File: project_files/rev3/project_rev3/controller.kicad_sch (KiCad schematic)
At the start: 26 parts, among them J8 USB_C_Receptacle_USB2.0_16P, SW1 JS102011SAQN, SW2 PTS810 SJM 250 SMTR LFS, SW3 PTS810 SJM 250 SMTR LFS, U5 ESP32-S3-WROOM-1-N16R8, U6 AZ1117CH-3.3

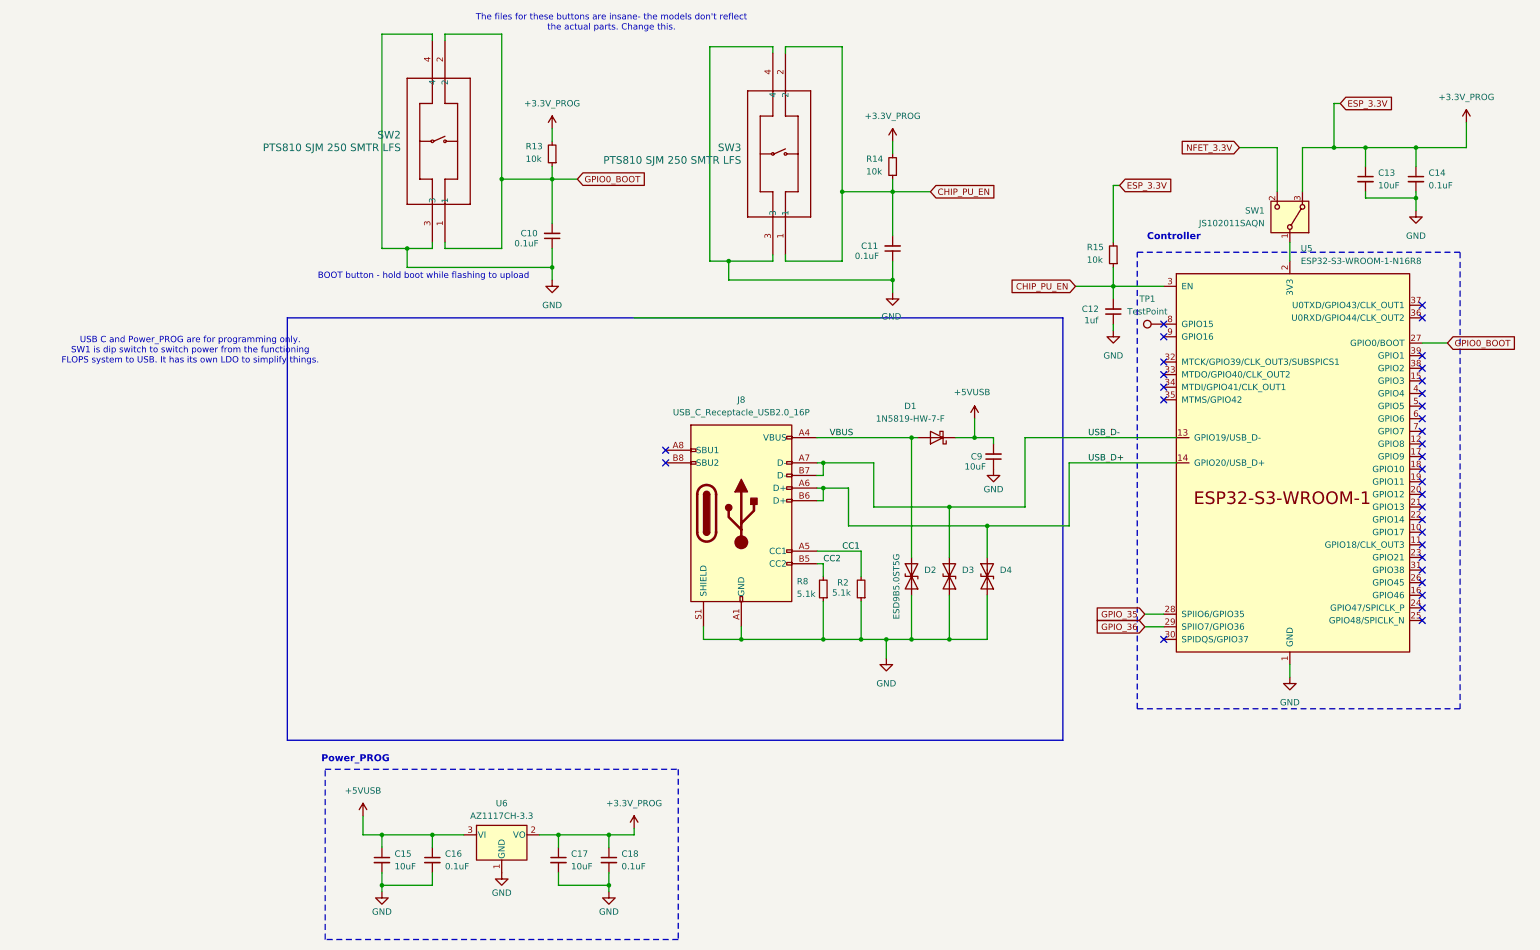
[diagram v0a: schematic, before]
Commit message: added new project for rev4 and reverted changes for rev3
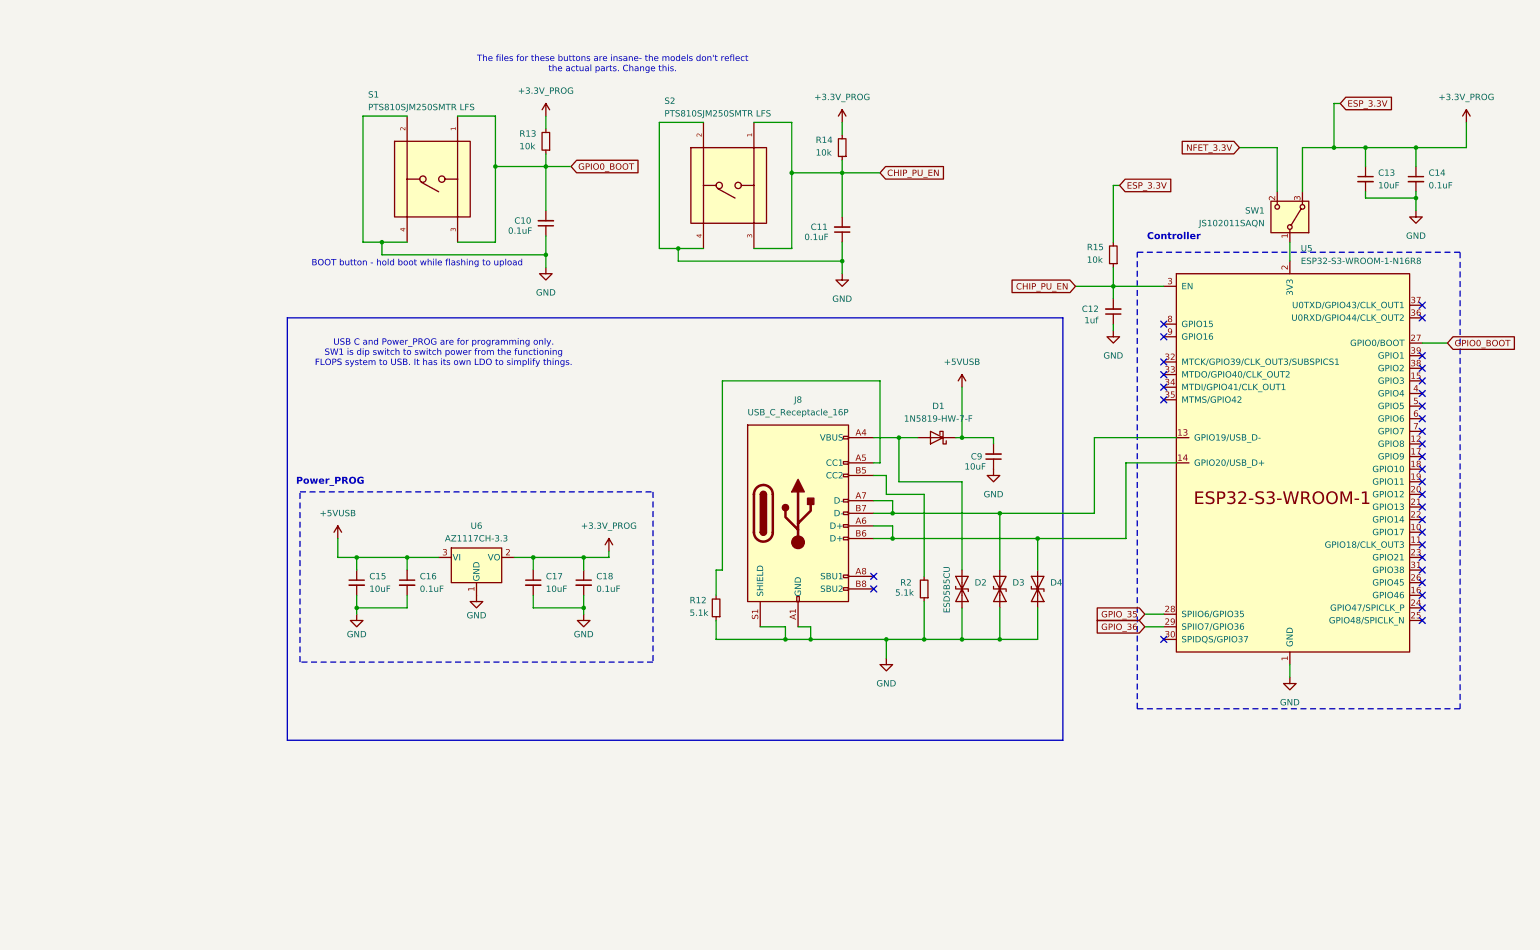
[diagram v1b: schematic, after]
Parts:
- removed R8: 5.1k, Resistor_SMD:R_0603_1608Metric_Pad0.98x0.95mm_HandSolder, symbol Device:R_Small
- removed SW2, SW3: PTS810 SJM 250 SMTR LFS, PTS810SJM250SMTR LFS:PTS810_CNK, symbol PTS810SJM250SMTR LFS:PTS810_SJM_250_SMTR_LFS
- removed TP1: TestPoint, symbol Connector:TestPoint
- added R12: 5.1k, Resistor_SMD:R_0603_1608Metric_Pad0.98x0.95mm_HandSolder, symbol Device:R_Small
- added S1, S2: PTS810SJM250SMTR LFS, TS04-66-95-BK-100-SMT:SW_TS04-66-95-BK-100-SMT, symbol TS04-66-95-BK-100-SMT:TS04-66-95-BK-100-SMT
- D1: footprint Diode_SMD:D_SOD-123 -> Diode_THT:D_DO-41_SOD81_P10.16mm_Horizontal
- D2, D3, D4: value ESD9B5.0ST5G -> ESD5B5CU
- J8: value USB_C_Receptacle_USB2.0_16P -> USB_C_Receptacle_16P; footprint Connector_USB:USB_C_Receptacle_GCT_USB4105-xx-A_16P_TopMnt_Horizontal -> Connector_USB:USB_C_Receptacle_G-Switch_GT-USB-7010ASV
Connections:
- net CC2 is gone; now on an unnamed net: J8.B5 (CC2)
- net CHIP_PU_EN: now also S2.1, S2.3
- net GND: now also R12.1, S1.2, S1.4, S2.2, S2.4
- net GPIO0_BOOT: now also S1.1, S1.3
- net CC1: no longer names the net of R2.2
- net CC1: no longer J8.A5 (CC1)
- net USB_D+: no longer names the net of D4.1 (A1), J8.A6 (D+), J8.B6 (D+), U5.14 (GPIO20/USB_D+)
- net USB_D-: no longer names the net of D3.1 (A1), J8.A7 (D-), J8.B7 (D-), U5.13 (GPIO19/USB_D-)
- net VBUS: no longer names the net of D1.2 (A), D2.1 (A1), J8.A4 (VBUS), J8.A9 (VBUS), J8.B4 (VBUS), J8.B9 (VBUS)
- new net: J8.A5 (CC1), R12.2
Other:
- moved on the sheet: C10, C11, C15, C16, C17, C18, D2, D3, D4, R13, R14, R2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
